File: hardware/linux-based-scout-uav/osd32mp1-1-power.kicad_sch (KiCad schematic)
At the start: 1 part, among them U1 OSD32MP157C-512M-IAA

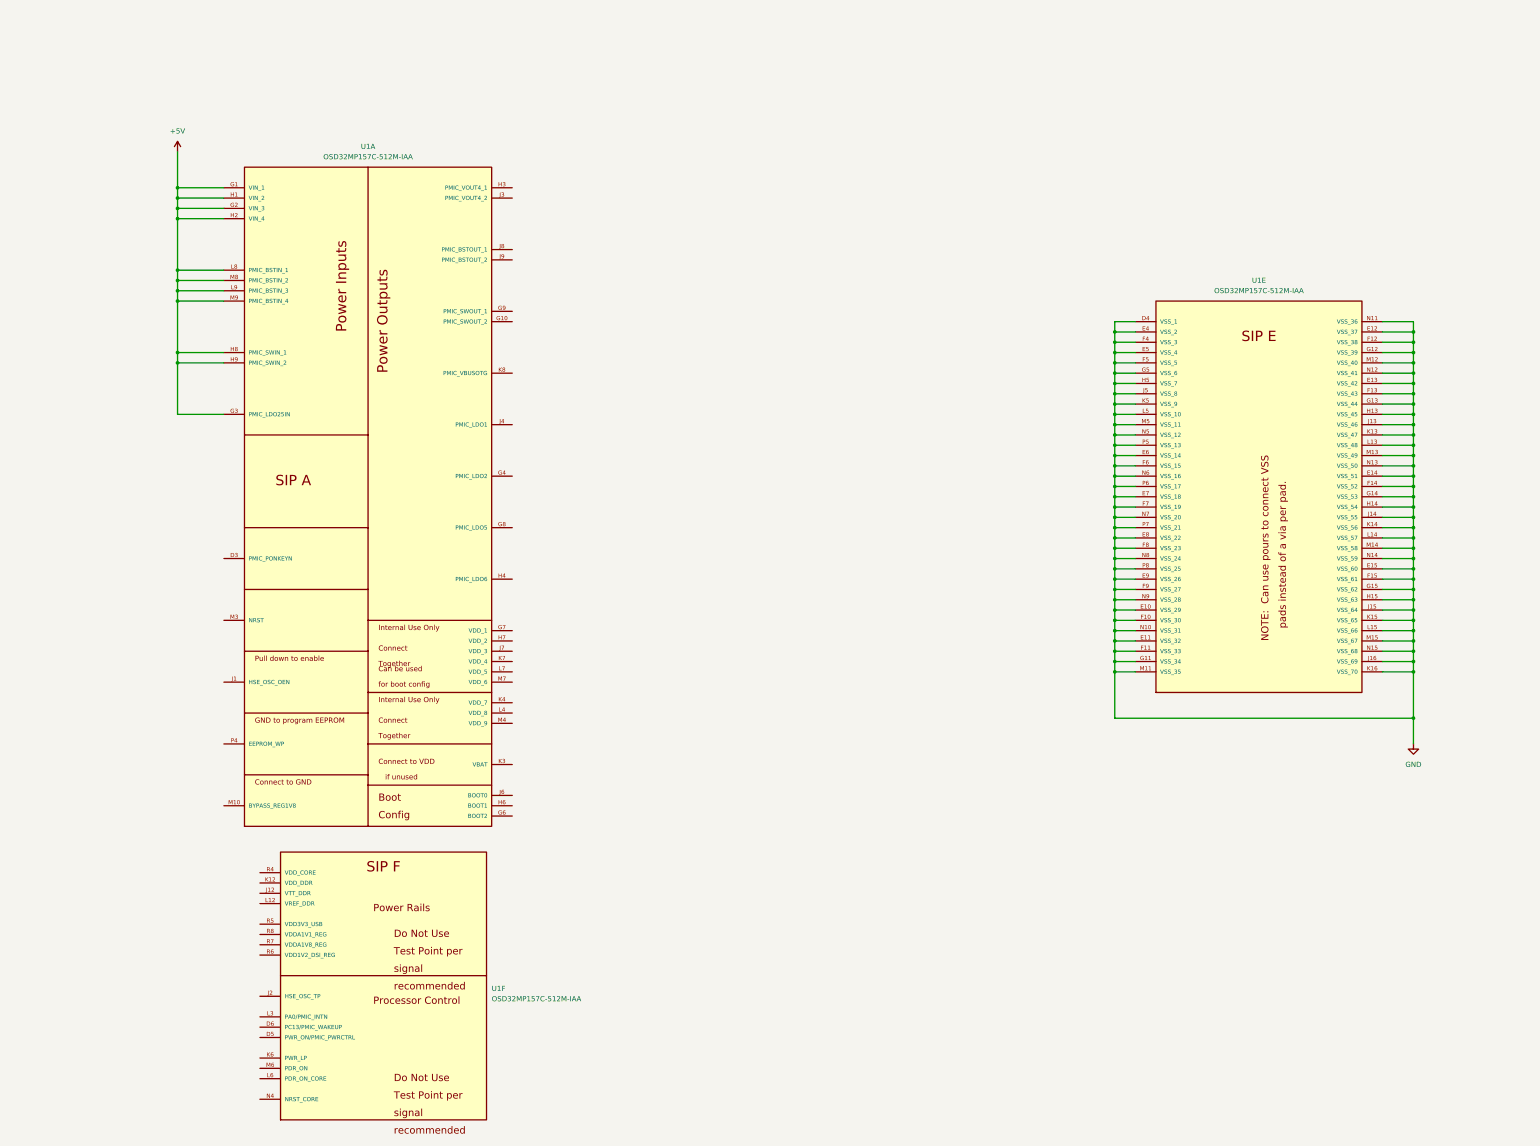
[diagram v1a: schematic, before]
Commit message: schematic update
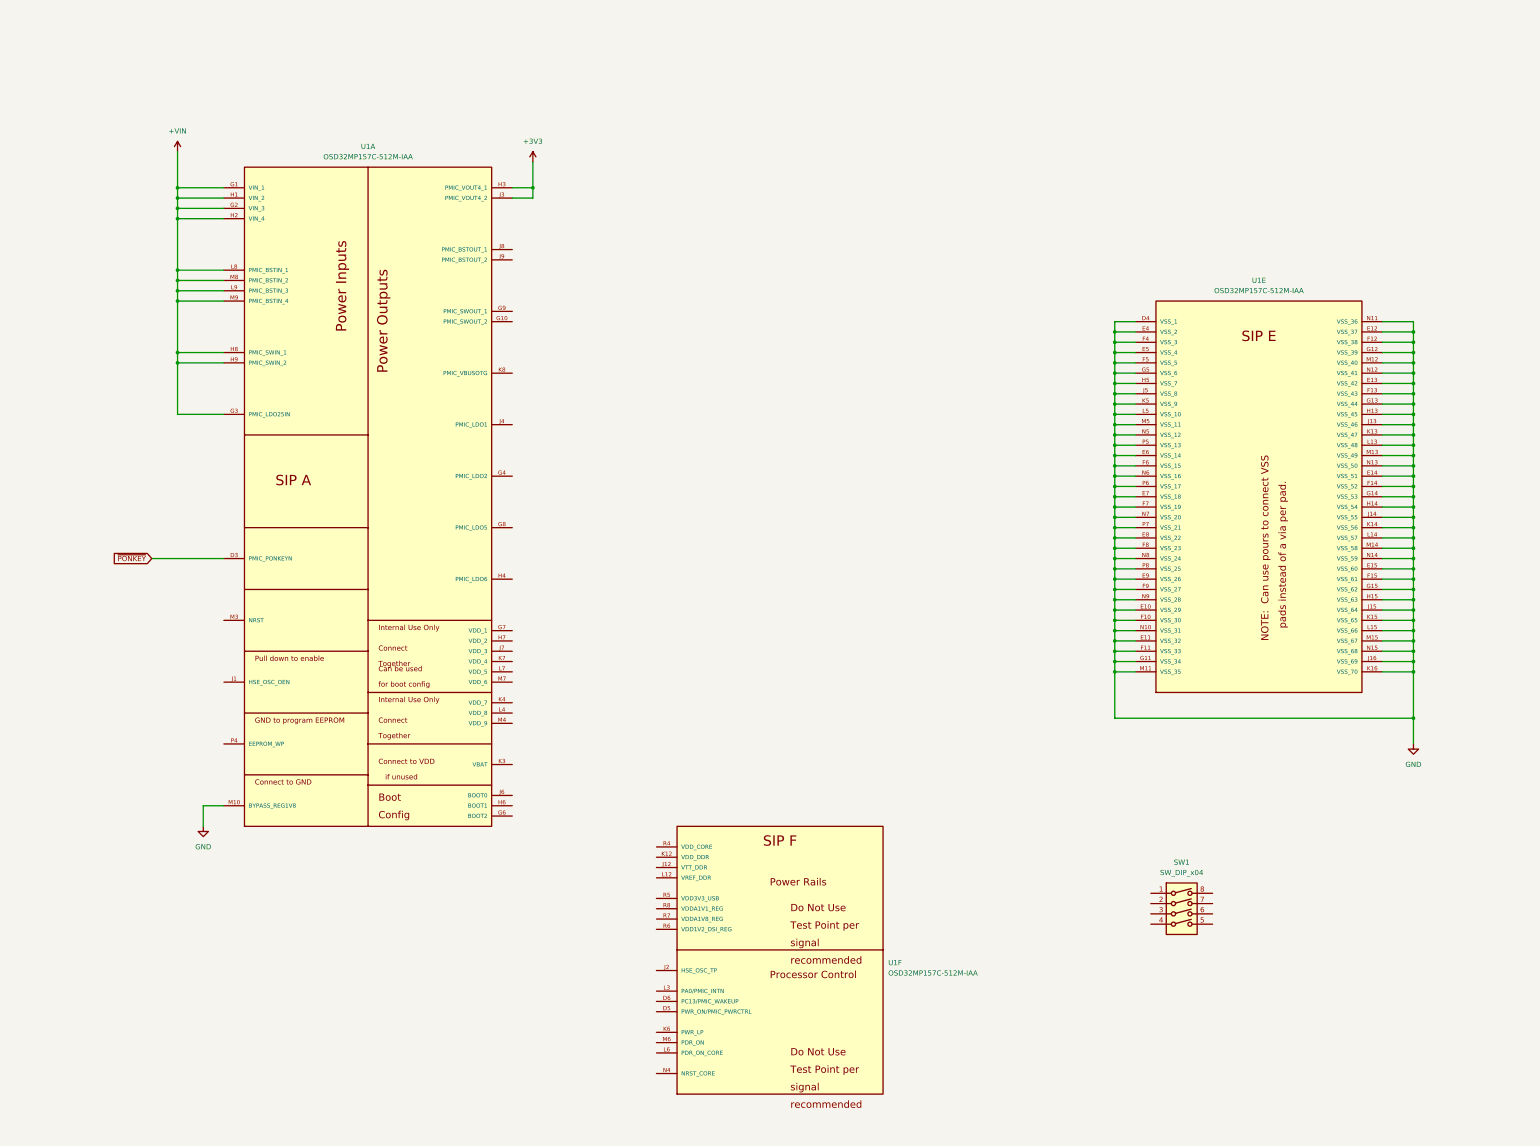
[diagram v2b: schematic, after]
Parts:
- added SW1: SW_DIP_x04, symbol Switch:SW_DIP_x04
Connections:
- net GND: now also U1.M10 (BYPASS_REG1V8)
- net ~{PONKEY}: now reaches U1.D3 (PMIC_PONKEYN)
- net +3V3: now reaches U1.H3 (PMIC_VOUT4_1)
- net +3V3: now also U1.J3 (PMIC_VOUT4_2)
- net +5V renamed +VIN
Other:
- moved on the sheet: U1F

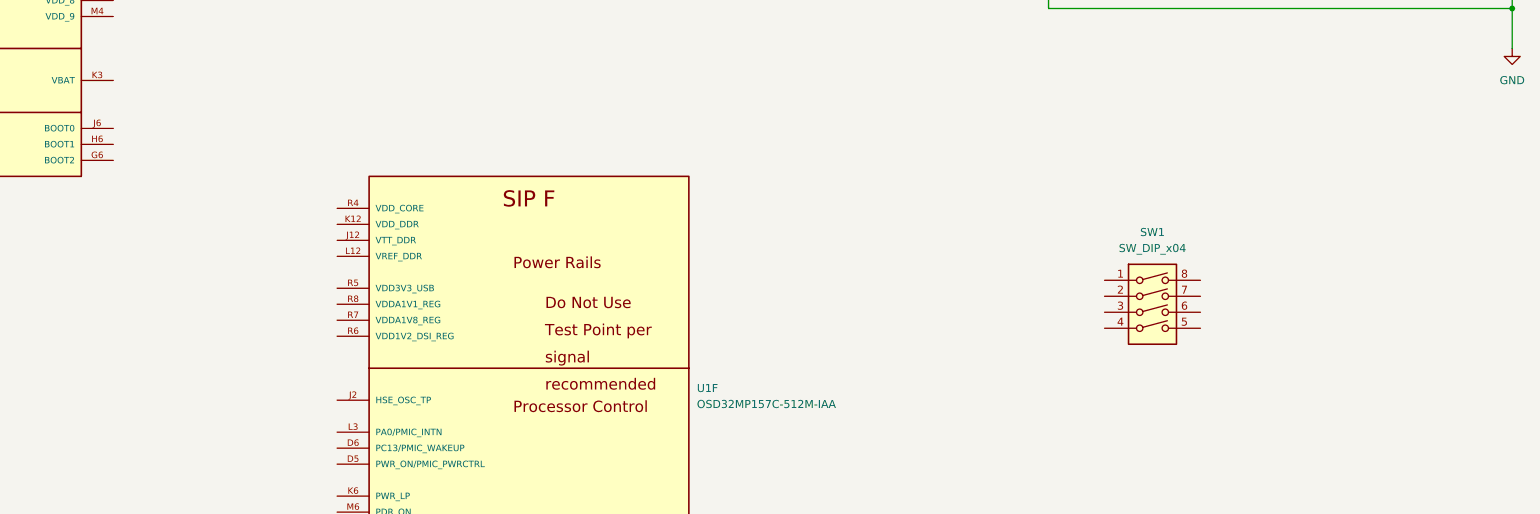
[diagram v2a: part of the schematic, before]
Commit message: Updates; schematic, readme, doc files
Schematic,  readme and doc files updates.
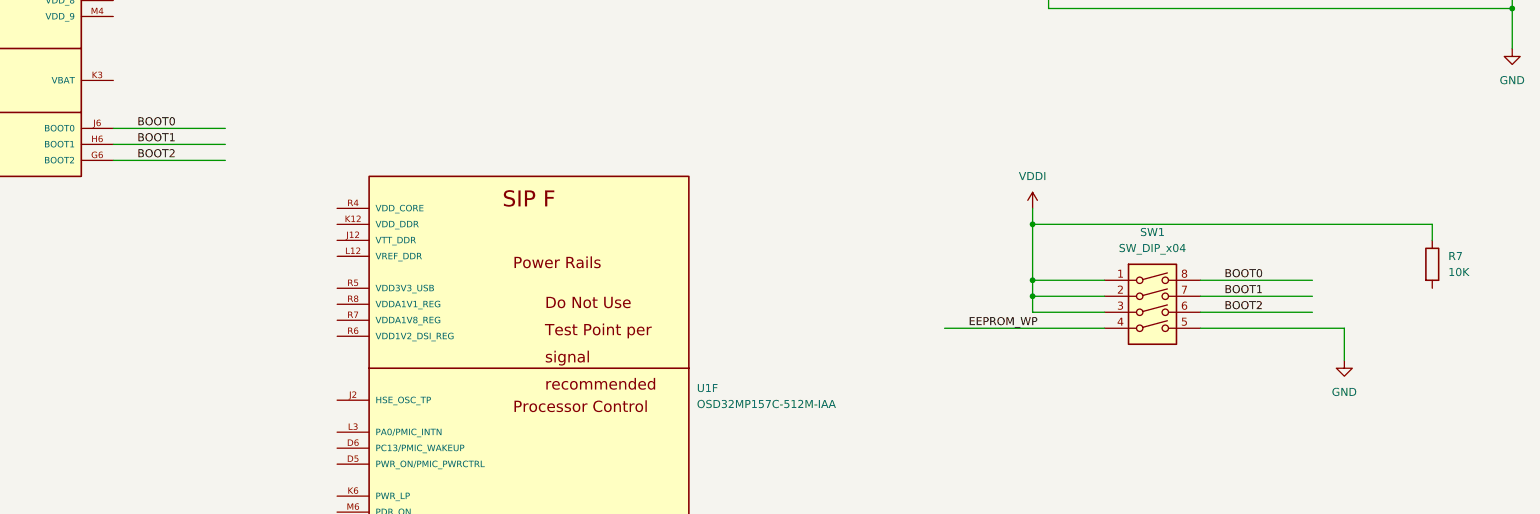
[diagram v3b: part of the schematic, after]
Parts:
- added R7: 10K, symbol Device:R
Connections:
- net GND: now also SW1.5
- net VDDI: now reaches SW1.1
- net VDDI: now also SW1.2, SW1.3, R7.1
- net EEPROM_WP: now reaches SW1.4
- net BOOT2: now reaches SW1.6
- net BOOT2: now also U1.G6 (BOOT2)
- net BOOT1: now reaches SW1.7
- net BOOT1: now also U1.H6 (BOOT1)
- net BOOT0: now reaches SW1.8
- net BOOT0: now also U1.J6 (BOOT0)

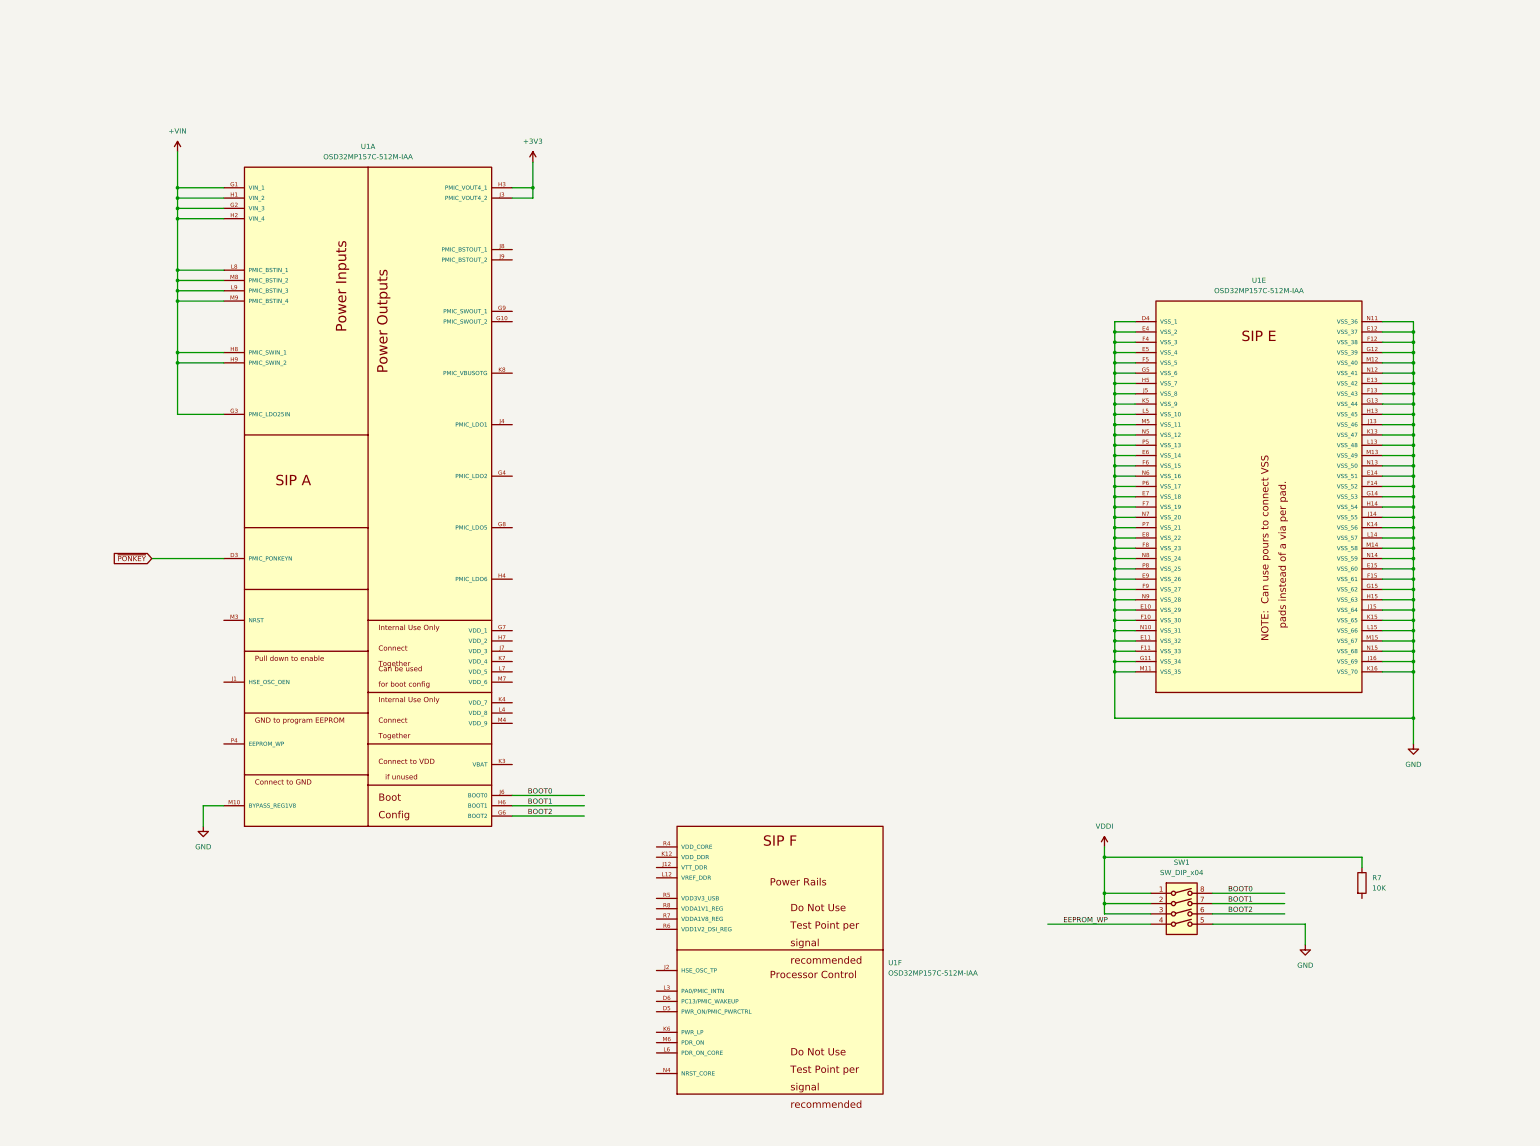
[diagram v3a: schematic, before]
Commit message: Schematic updates
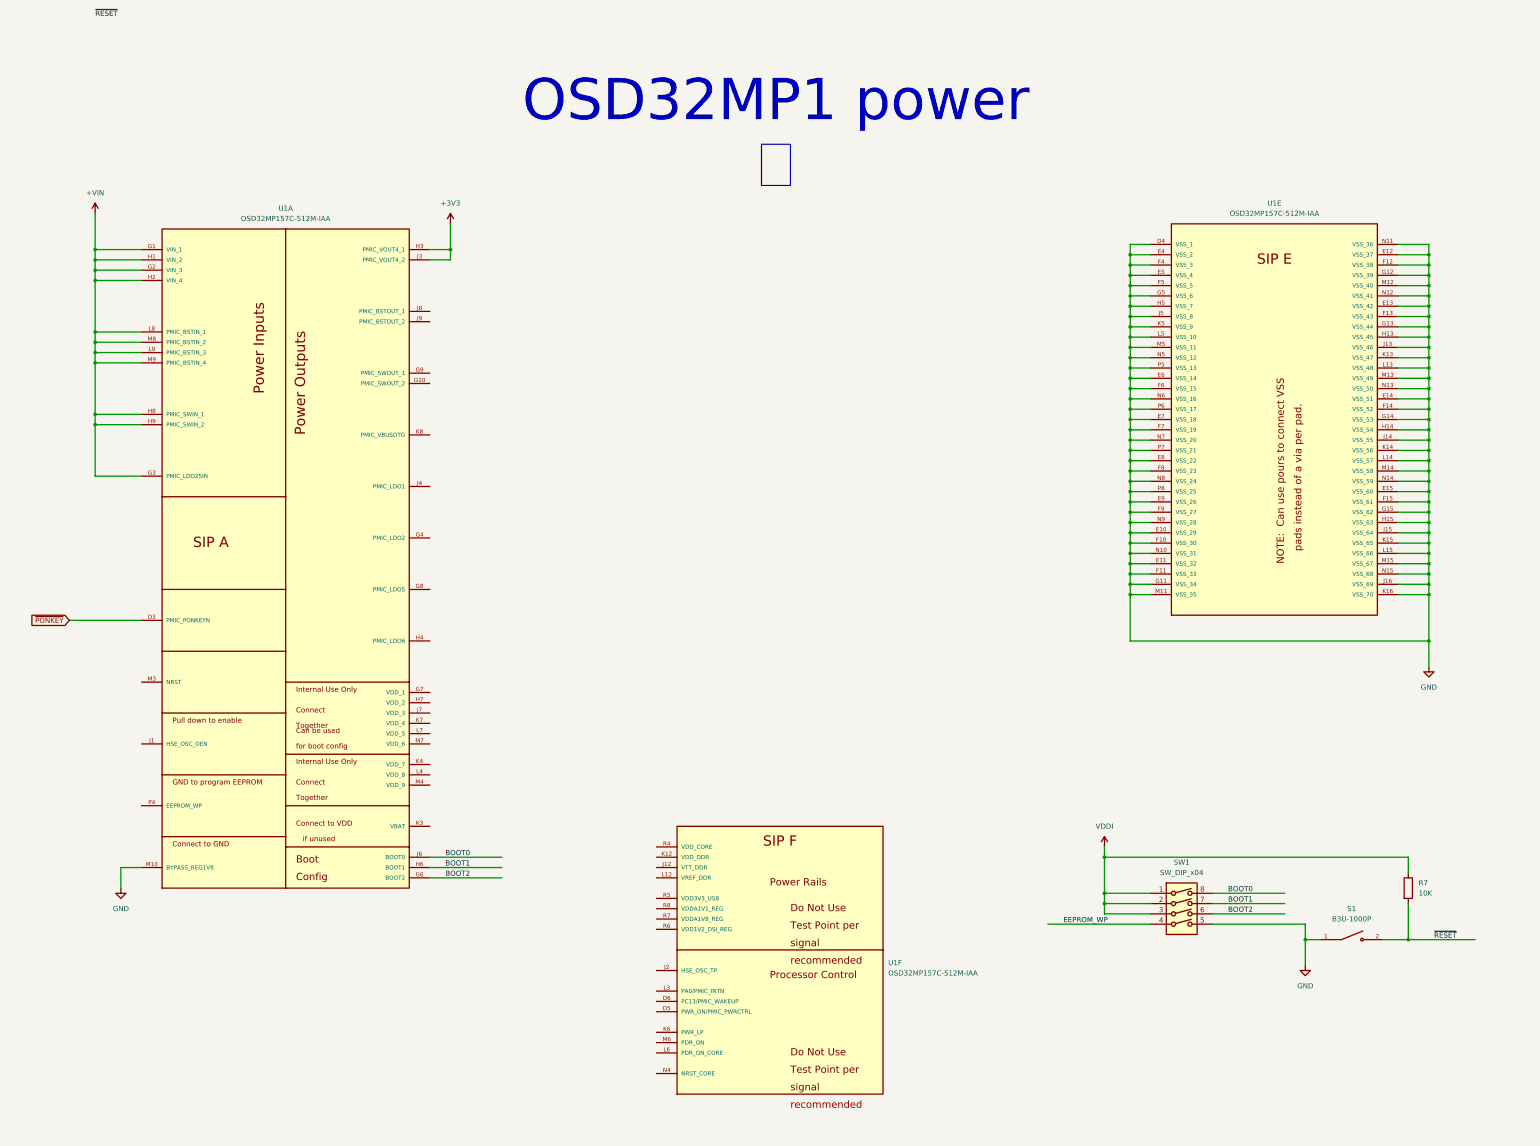
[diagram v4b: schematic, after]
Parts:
- added S1: B3U-1000P, B3U-1000P:SW_B3U-1000P, symbol B3U-1000P:B3U-1000P
- R7: footprint (none) -> Resistor_SMD:R_0402_1005Metric
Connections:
- net GND: now also S1.1
- net ~{RESET}: now reaches R7.2
- net ~{RESET}: now also S1.2
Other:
- note added: "OSD32MP1 power 力"
- moved on the sheet: R7, U1A, U1E

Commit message: Schematic update
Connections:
- net VDDI: now also U1.G7 (VDD_1), U1.H7 (VDD_2), U1.J7 (VDD_3), U1.K4 (VDD_7), U1.K7 (VDD_4), U1.L4 (VDD_8), U1.L7 (VDD_5), U1.M4 (VDD_9), U1.M7 (VDD_6)
- net +VSW: now reaches U1.G10 (PMIC_SWOUT_2)
- net +VSW: now also U1.G9 (PMIC_SWOUT_1)
- net +VLDO2: now reaches U1.G4 (PMIC_LDO2)
- net +BST: now reaches U1.J8 (PMIC_BSTOUT_1)
- net +BST: now also U1.J9 (PMIC_BSTOUT_2)

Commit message: Schematic update
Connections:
- net EEPROM_WP: now also U1.P4 (EEPROM_WP)
- net GND: now also U1.J1 (HSE_OSC_OEN)
- net ~{RESET}: now also U1.M3 (NRST)
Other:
- note added: "User config and reset control"
- moved on the sheet: R7, S1, SW1

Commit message: Schematic update
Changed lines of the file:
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@@
+		)
+	)
+	(global_label "~{RESET}"
+		(shape passive)
+		(at 40.64 165.1 180)
+		(fields_autoplaced yes)
+		(effects
+			(font
+				(size 1.27 1.27)
+			)
+			(justify right)
+		)
+		(property "Intersheetrefs" "${INTERSHEET_REFS}"
+			(at 33.021 165.1 0)
+			(effects
+				(font
+					(size 1.27 1.27)
+				)
+				(justify right)
+				(hide yes)
+			)
 		)
 	)
